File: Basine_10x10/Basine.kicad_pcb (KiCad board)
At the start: 2 copper layers, 100 x 100 mm, 56 parts, among them J1 2060-451/998-404, J10 2060-451/998-404, J11 2060-451/998-404, J12 2060-451/998-404, J13 2060-451/998-404, J14 2060-451/998-404, J15 2060-451/998-404, J16 2060-451/998-404, J17 2060-451/998-404, J18 2060-451/998-404, J2 2060-451/998-404, J3 2060-451/998-404, J4 2060-451/998-404, J5 2060-451/998-404, J6 2060-451/998-404, J7 2060-451/998-404, J8 2060-451/998-404, J9 2060-451/998-404

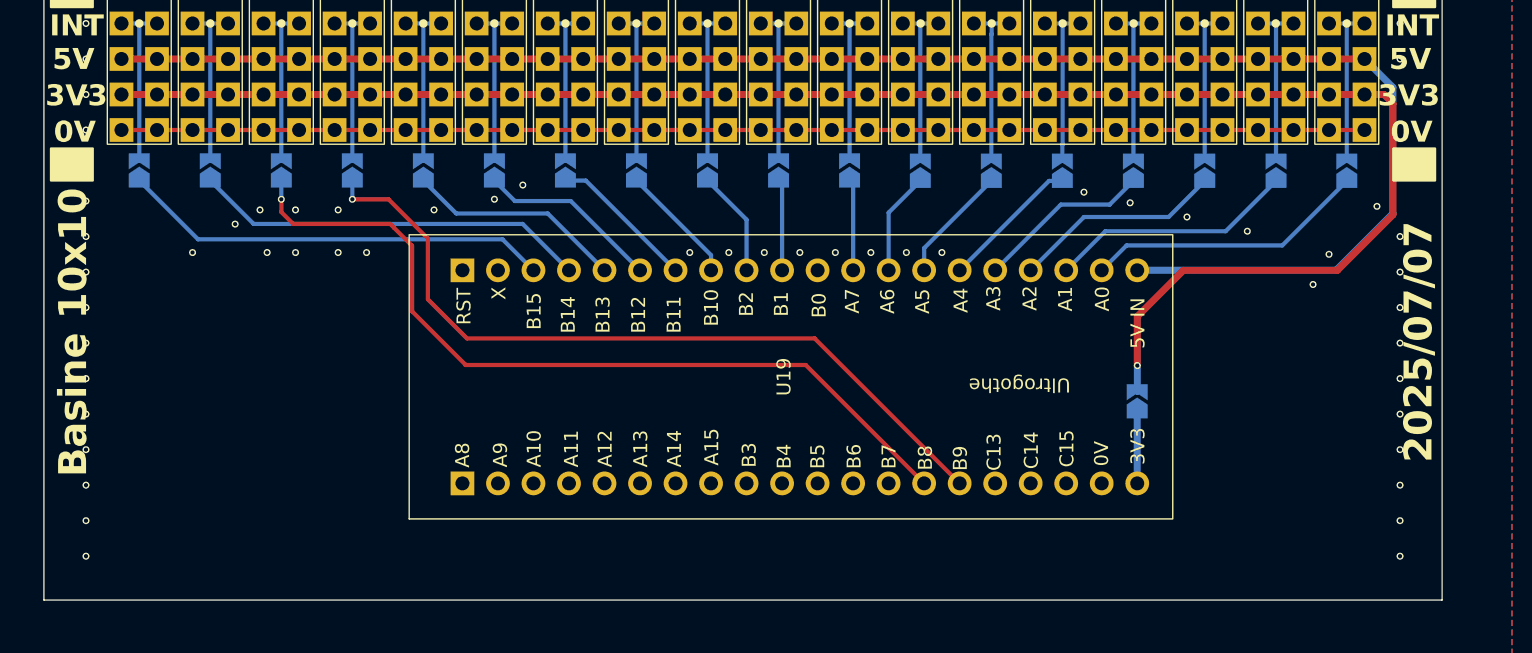
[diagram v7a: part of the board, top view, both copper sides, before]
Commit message: Basine_10x10 : recentrage ultro et ajout zone proto
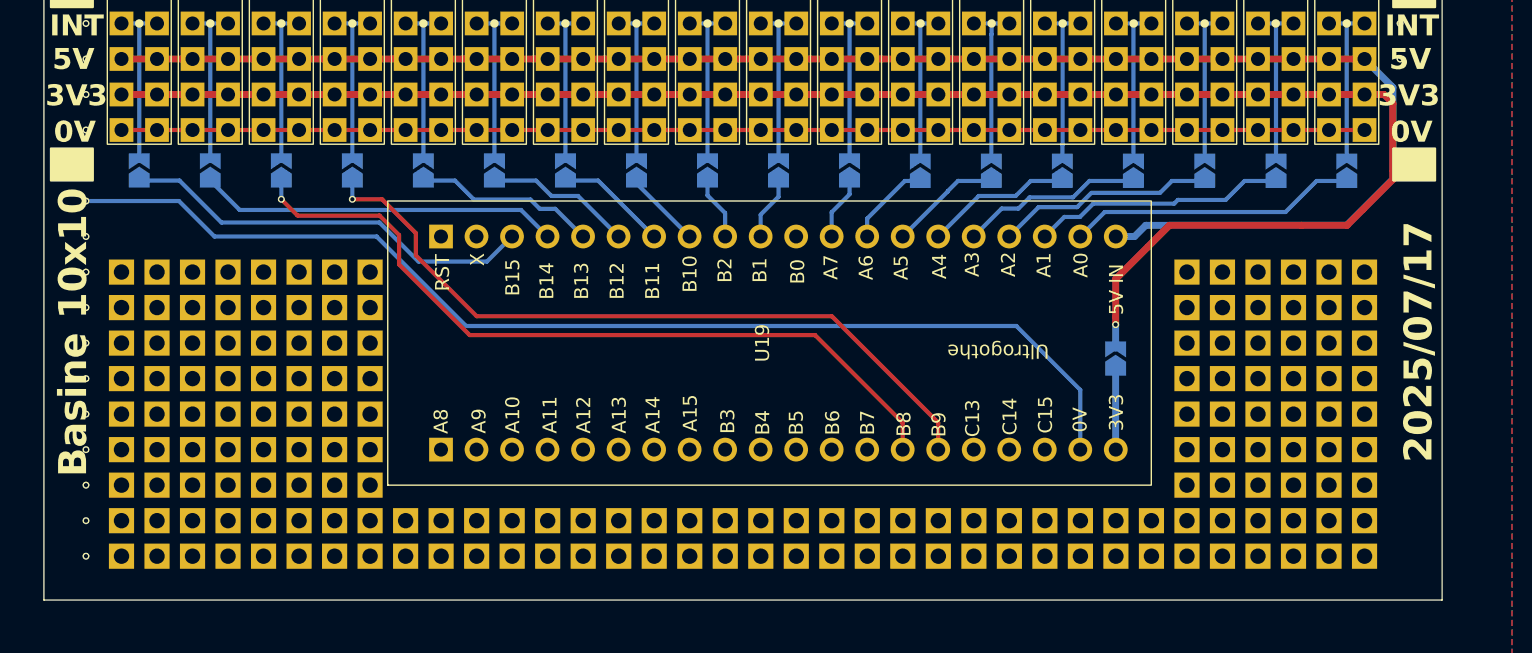
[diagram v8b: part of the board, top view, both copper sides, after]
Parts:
- added J100: Pastille, Chimere_comps:Pastille_carree, F.Cu at (146.2, 194.3)
- added J101: Pastille, Chimere_comps:Pastille_carree, F.Cu at (148.7, 194.3)
- added J102: Pastille, Chimere_comps:Pastille_carree, F.Cu at (151.3, 194.3)
- added J103: Pastille, Chimere_comps:Pastille_carree, F.Cu at (153.8, 194.3)
- added J104: Pastille, Chimere_comps:Pastille_carree, F.Cu at (156.3, 194.3)
- added J105: Pastille, Chimere_comps:Pastille_carree, F.Cu at (158.9, 194.3)
- added J106: Pastille, Chimere_comps:Pastille_carree, F.Cu at (161.4, 194.3)
- added J107: Pastille, Chimere_comps:Pastille_carree, F.Cu at (164.0, 194.3)
- added J108: Pastille, Chimere_comps:Pastille_carree, F.Cu at (166.5, 194.3)
- added J109: Pastille, Chimere_comps:Pastille_carree, F.Cu at (169.1, 194.3)
- added J110: Pastille, Chimere_comps:Pastille_carree, F.Cu at (171.6, 194.3)
- added J111: Pastille, Chimere_comps:Pastille_carree, F.Cu at (174.1, 194.3)
- added J112: Pastille, Chimere_comps:Pastille_carree, F.Cu at (176.7, 194.3)
- added J113: Pastille, Chimere_comps:Pastille_carree, F.Cu at (179.2, 194.3)
- added J114: Pastille, Chimere_comps:Pastille_carree, F.Cu at (125.9, 196.9)
- added J115: Pastille, Chimere_comps:Pastille_carree, F.Cu at (128.4, 196.9)
- added J116: Pastille, Chimere_comps:Pastille_carree, F.Cu at (130.9, 196.9)
- added J117: Pastille, Chimere_comps:Pastille_carree, F.Cu at (133.5, 196.9)
- added J118: Pastille, Chimere_comps:Pastille_carree, F.Cu at (136.0, 196.9)
- added J119: Pastille, Chimere_comps:Pastille_carree, F.Cu at (138.6, 196.9)
- added J120: Pastille, Chimere_comps:Pastille_carree, F.Cu at (141.1, 196.9)
- added J121: Pastille, Chimere_comps:Pastille_carree, F.Cu at (143.7, 196.9)
- added J122: Pastille, Chimere_comps:Pastille_carree, F.Cu at (146.2, 196.9)
- added J123: Pastille, Chimere_comps:Pastille_carree, F.Cu at (148.7, 196.9)
- added J124: Pastille, Chimere_comps:Pastille_carree, F.Cu at (151.3, 196.9)
- added J125: Pastille, Chimere_comps:Pastille_carree, F.Cu at (153.8, 196.9)
- added J126: Pastille, Chimere_comps:Pastille_carree, F.Cu at (156.3, 196.9)
- added J127: Pastille, Chimere_comps:Pastille_carree, F.Cu at (158.9, 196.9)
- added J128: Pastille, Chimere_comps:Pastille_carree, F.Cu at (161.4, 196.9)
- added J129: Pastille, Chimere_comps:Pastille_carree, F.Cu at (164.0, 196.9)
- added J130: Pastille, Chimere_comps:Pastille_carree, F.Cu at (166.5, 196.9)
- added J131: Pastille, Chimere_comps:Pastille_carree, F.Cu at (169.1, 196.9)
- added J132: Pastille, Chimere_comps:Pastille_carree, F.Cu at (171.6, 196.9)
- added J133: Pastille, Chimere_comps:Pastille_carree, F.Cu at (174.1, 196.9)
- added J134: Pastille, Chimere_comps:Pastille_carree, F.Cu at (176.7, 196.9)
- added J135: Pastille, Chimere_comps:Pastille_carree, F.Cu at (194.4, 196.9)
- added J136: Pastille, Chimere_comps:Pastille_carree, F.Cu at (181.8, 176.5)
- added J137: Pastille, Chimere_comps:Pastille_carree, F.Cu at (184.3, 176.5)
- added J138: Pastille, Chimere_comps:Pastille_carree, F.Cu at (186.8, 176.5)
- added J139: Pastille, Chimere_comps:Pastille_carree, F.Cu at (189.4, 176.5)
- added J140: Pastille, Chimere_comps:Pastille_carree, F.Cu at (191.9, 176.5)
- added J141: Pastille, Chimere_comps:Pastille_carree, F.Cu at (194.4, 176.5)
- added J142: Pastille, Chimere_comps:Pastille_carree, F.Cu at (181.8, 179.1)
- added J143: Pastille, Chimere_comps:Pastille_carree, F.Cu at (184.3, 179.1)
- added J144: Pastille, Chimere_comps:Pastille_carree, F.Cu at (186.8, 179.1)
- added J145: Pastille, Chimere_comps:Pastille_carree, F.Cu at (189.4, 179.1)
- added J146: Pastille, Chimere_comps:Pastille_carree, F.Cu at (191.9, 179.1)
- added J147: Pastille, Chimere_comps:Pastille_carree, F.Cu at (194.4, 179.1)
- added J148: Pastille, Chimere_comps:Pastille_carree, F.Cu at (181.8, 181.6)
- added J149: Pastille, Chimere_comps:Pastille_carree, F.Cu at (184.3, 181.6)
- added J150: Pastille, Chimere_comps:Pastille_carree, F.Cu at (186.8, 181.6)
- added J151: Pastille, Chimere_comps:Pastille_carree, F.Cu at (189.4, 181.6)
- added J152: Pastille, Chimere_comps:Pastille_carree, F.Cu at (191.9, 181.6)
- added J153: Pastille, Chimere_comps:Pastille_carree, F.Cu at (194.4, 181.6)
- added J154: Pastille, Chimere_comps:Pastille_carree, F.Cu at (181.8, 184.2)
- added J155: Pastille, Chimere_comps:Pastille_carree, F.Cu at (184.3, 184.2)
- added J156: Pastille, Chimere_comps:Pastille_carree, F.Cu at (186.8, 184.2)
- added J157: Pastille, Chimere_comps:Pastille_carree, F.Cu at (189.4, 184.2)
- added J158: Pastille, Chimere_comps:Pastille_carree, F.Cu at (191.9, 184.2)
- added J159: Pastille, Chimere_comps:Pastille_carree, F.Cu at (194.4, 184.2)
- added J160: Pastille, Chimere_comps:Pastille_carree, F.Cu at (181.8, 186.7)
- added J161: Pastille, Chimere_comps:Pastille_carree, F.Cu at (184.3, 186.7)
- added J162: Pastille, Chimere_comps:Pastille_carree, F.Cu at (186.8, 186.7)
- added J163: Pastille, Chimere_comps:Pastille_carree, F.Cu at (189.4, 186.7)
- added J164: Pastille, Chimere_comps:Pastille_carree, F.Cu at (191.9, 186.7)
- added J165: Pastille, Chimere_comps:Pastille_carree, F.Cu at (194.4, 186.7)
- added J166: Pastille, Chimere_comps:Pastille_carree, F.Cu at (181.8, 189.2)
- added J167: Pastille, Chimere_comps:Pastille_carree, F.Cu at (184.3, 189.2)
- added J168: Pastille, Chimere_comps:Pastille_carree, F.Cu at (186.8, 189.2)
- added J169: Pastille, Chimere_comps:Pastille_carree, F.Cu at (189.4, 189.2)
- added J170: Pastille, Chimere_comps:Pastille_carree, F.Cu at (191.9, 189.2)
- added J171: Pastille, Chimere_comps:Pastille_carree, F.Cu at (194.4, 189.2)
- added J172: Pastille, Chimere_comps:Pastille_carree, F.Cu at (181.8, 191.8)
- added J173: Pastille, Chimere_comps:Pastille_carree, F.Cu at (184.3, 191.8)
- added J174: Pastille, Chimere_comps:Pastille_carree, F.Cu at (186.8, 191.8)
- added J175: Pastille, Chimere_comps:Pastille_carree, F.Cu at (189.4, 191.8)
- added J176: Pastille, Chimere_comps:Pastille_carree, F.Cu at (191.9, 191.8)
- added J177: Pastille, Chimere_comps:Pastille_carree, F.Cu at (194.4, 191.8)
- added J178: Pastille, Chimere_comps:Pastille_carree, F.Cu at (181.8, 194.3)
- added J179: Pastille, Chimere_comps:Pastille_carree, F.Cu at (184.3, 194.3)
- added J180: Pastille, Chimere_comps:Pastille_carree, F.Cu at (186.8, 194.3)
- added J181: Pastille, Chimere_comps:Pastille_carree, F.Cu at (189.4, 194.3)
- added J182: Pastille, Chimere_comps:Pastille_carree, F.Cu at (191.9, 194.3)
- added J183: Pastille, Chimere_comps:Pastille_carree, F.Cu at (194.4, 194.3)
- added J184: Pastille, Chimere_comps:Pastille_carree, F.Cu at (181.8, 196.9)
- added J185: Pastille, Chimere_comps:Pastille_carree, F.Cu at (184.3, 196.9)
- added J186: Pastille, Chimere_comps:Pastille_carree, F.Cu at (186.8, 196.9)
- added J187: Pastille, Chimere_comps:Pastille_carree, F.Cu at (189.4, 196.9)
- added J188: Pastille, Chimere_comps:Pastille_carree, F.Cu at (191.9, 196.9)
- added J19: Pastille, Chimere_comps:Pastille_carree, F.Cu at (123.3, 196.9)
- added J20: Pastille, Chimere_comps:Pastille_carree, F.Cu at (105.5, 176.5)
- added J21: Pastille, Chimere_comps:Pastille_carree, F.Cu at (108.1, 176.5)
- added J22: Pastille, Chimere_comps:Pastille_carree, F.Cu at (110.6, 176.5)
- added J23: Pastille, Chimere_comps:Pastille_carree, F.Cu at (113.2, 176.5)
- added J24: Pastille, Chimere_comps:Pastille_carree, F.Cu at (115.7, 176.5)
- added J25: Pastille, Chimere_comps:Pastille_carree, F.Cu at (118.2, 176.5)
- added J26: Pastille, Chimere_comps:Pastille_carree, F.Cu at (120.8, 176.5)
- added J27: Pastille, Chimere_comps:Pastille_carree, F.Cu at (123.3, 176.5)
- added J28: Pastille, Chimere_comps:Pastille_carree, F.Cu at (105.5, 179.1)
- added J29: Pastille, Chimere_comps:Pastille_carree, F.Cu at (108.1, 179.1)
- added J30: Pastille, Chimere_comps:Pastille_carree, F.Cu at (110.6, 179.1)
- added J31: Pastille, Chimere_comps:Pastille_carree, F.Cu at (113.2, 179.1)
- added J32: Pastille, Chimere_comps:Pastille_carree, F.Cu at (115.7, 179.1)
- added J33: Pastille, Chimere_comps:Pastille_carree, F.Cu at (118.2, 179.1)
- added J34: Pastille, Chimere_comps:Pastille_carree, F.Cu at (120.8, 179.1)
- added J35: Pastille, Chimere_comps:Pastille_carree, F.Cu at (123.3, 179.1)
- added J36: Pastille, Chimere_comps:Pastille_carree, F.Cu at (105.5, 181.6)
- added J37: Pastille, Chimere_comps:Pastille_carree, F.Cu at (108.1, 181.6)
- added J38: Pastille, Chimere_comps:Pastille_carree, F.Cu at (110.6, 181.6)
- added J39: Pastille, Chimere_comps:Pastille_carree, F.Cu at (113.2, 181.6)
- added J40: Pastille, Chimere_comps:Pastille_carree, F.Cu at (115.7, 181.6)
- added J41: Pastille, Chimere_comps:Pastille_carree, F.Cu at (118.2, 181.6)
- added J42: Pastille, Chimere_comps:Pastille_carree, F.Cu at (120.8, 181.6)
- added J43: Pastille, Chimere_comps:Pastille_carree, F.Cu at (123.3, 181.6)
- added J44: Pastille, Chimere_comps:Pastille_carree, F.Cu at (105.5, 184.2)
- added J45: Pastille, Chimere_comps:Pastille_carree, F.Cu at (108.1, 184.2)
- added J46: Pastille, Chimere_comps:Pastille_carree, F.Cu at (110.6, 184.2)
- added J47: Pastille, Chimere_comps:Pastille_carree, F.Cu at (113.2, 184.2)
- added J48: Pastille, Chimere_comps:Pastille_carree, F.Cu at (115.7, 184.2)
- added J49: Pastille, Chimere_comps:Pastille_carree, F.Cu at (118.2, 184.2)
- added J50: Pastille, Chimere_comps:Pastille_carree, F.Cu at (120.8, 184.2)
- added J51: Pastille, Chimere_comps:Pastille_carree, F.Cu at (123.3, 184.2)
- added J52: Pastille, Chimere_comps:Pastille_carree, F.Cu at (105.5, 186.7)
- added J53: Pastille, Chimere_comps:Pastille_carree, F.Cu at (108.1, 186.7)
- added J54: Pastille, Chimere_comps:Pastille_carree, F.Cu at (110.6, 186.7)
- added J55: Pastille, Chimere_comps:Pastille_carree, F.Cu at (113.2, 186.7)
- added J56: Pastille, Chimere_comps:Pastille_carree, F.Cu at (115.7, 186.7)
- added J57: Pastille, Chimere_comps:Pastille_carree, F.Cu at (118.2, 186.7)
- added J58: Pastille, Chimere_comps:Pastille_carree, F.Cu at (120.8, 186.7)
- added J59: Pastille, Chimere_comps:Pastille_carree, F.Cu at (123.3, 186.7)
- added J60: Pastille, Chimere_comps:Pastille_carree, F.Cu at (105.5, 189.2)
- added J61: Pastille, Chimere_comps:Pastille_carree, F.Cu at (108.1, 189.2)
- added J62: Pastille, Chimere_comps:Pastille_carree, F.Cu at (110.6, 189.2)
- added J63: Pastille, Chimere_comps:Pastille_carree, F.Cu at (113.2, 189.2)
- added J64: Pastille, Chimere_comps:Pastille_carree, F.Cu at (115.7, 189.2)
- added J65: Pastille, Chimere_comps:Pastille_carree, F.Cu at (118.2, 189.2)
- added J66: Pastille, Chimere_comps:Pastille_carree, F.Cu at (120.8, 189.2)
- added J67: Pastille, Chimere_comps:Pastille_carree, F.Cu at (123.3, 189.2)
- added J68: Pastille, Chimere_comps:Pastille_carree, F.Cu at (105.5, 191.8)
- added J69: Pastille, Chimere_comps:Pastille_carree, F.Cu at (108.1, 191.8)
- added J70: Pastille, Chimere_comps:Pastille_carree, F.Cu at (110.6, 191.8)
- added J71: Pastille, Chimere_comps:Pastille_carree, F.Cu at (113.2, 191.8)
- added J72: Pastille, Chimere_comps:Pastille_carree, F.Cu at (115.7, 191.8)
- added J73: Pastille, Chimere_comps:Pastille_carree, F.Cu at (118.2, 191.8)
- added J74: Pastille, Chimere_comps:Pastille_carree, F.Cu at (120.8, 191.8)
- added J75: Pastille, Chimere_comps:Pastille_carree, F.Cu at (123.3, 191.8)
- added J76: Pastille, Chimere_comps:Pastille_carree, F.Cu at (105.5, 194.3)
- added J77: Pastille, Chimere_comps:Pastille_carree, F.Cu at (108.1, 194.3)
- added J78: Pastille, Chimere_comps:Pastille_carree, F.Cu at (110.6, 194.3)
- added J79: Pastille, Chimere_comps:Pastille_carree, F.Cu at (113.2, 194.3)
- added J80: Pastille, Chimere_comps:Pastille_carree, F.Cu at (115.7, 194.3)
- added J81: Pastille, Chimere_comps:Pastille_carree, F.Cu at (118.2, 194.3)
- added J82: Pastille, Chimere_comps:Pastille_carree, F.Cu at (120.8, 194.3)
- added J83: Pastille, Chimere_comps:Pastille_carree, F.Cu at (123.3, 194.3)
- added J84: Pastille, Chimere_comps:Pastille_carree, F.Cu at (105.5, 196.9)
- added J85: Pastille, Chimere_comps:Pastille_carree, F.Cu at (108.1, 196.9)
- added J86: Pastille, Chimere_comps:Pastille_carree, F.Cu at (110.6, 196.9)
- added J87: Pastille, Chimere_comps:Pastille_carree, F.Cu at (113.2, 196.9)
- added J88: Pastille, Chimere_comps:Pastille_carree, F.Cu at (115.7, 196.9)
- added J89: Pastille, Chimere_comps:Pastille_carree, F.Cu at (118.2, 196.9)
- added J90: Pastille, Chimere_comps:Pastille_carree, F.Cu at (120.8, 196.9)
- added J91: Pastille, Chimere_comps:Pastille_carree, F.Cu at (179.2, 196.9)
- added J92: Pastille, Chimere_comps:Pastille_carree, F.Cu at (125.9, 194.3)
- added J93: Pastille, Chimere_comps:Pastille_carree, F.Cu at (128.4, 194.3)
- added J94: Pastille, Chimere_comps:Pastille_carree, F.Cu at (130.9, 194.3)
- added J95: Pastille, Chimere_comps:Pastille_carree, F.Cu at (133.5, 194.3)
- added J96: Pastille, Chimere_comps:Pastille_carree, F.Cu at (136.0, 194.3)
- added J97: Pastille, Chimere_comps:Pastille_carree, F.Cu at (138.6, 194.3)
- added J98: Pastille, Chimere_comps:Pastille_carree, F.Cu at (141.1, 194.3)
- added J99: Pastille, Chimere_comps:Pastille_carree, F.Cu at (143.7, 194.3)
- moved JP19 3.43 mm to (176.7, 182.7)
- moved U19 2.86 mm to (151.9, 181.6)
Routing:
- net 0V: track 197.9 -> 278.9 mm, vias 99 -> 62
- net CAN_RX: track 59.0 -> 55.5 mm
- net B10: track 8.63 -> 5.57 mm
- net B2: track 7.57 -> 4.52 mm
- net CAN_TX: track 55.7 -> 52.7 mm
- net B11: track 10.5 -> 8.00 mm
- net B12: track 13.1 -> 10.5 mm
- net B14: track 28.3 -> 25.8 mm
- net B13: track 15.6 -> 13.1 mm
- net A7: track 6.52 -> 4.89 mm
- net B1: track 6.52 -> 4.89 mm
- net 3V3: track 125.8 -> 124.4 mm
- net A6: track 7.33 -> 6.20 mm
- net B15: track 30.9 -> 29.8 mm
- net 5V: track 120.8 -> 119.9 mm
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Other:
- board text added: "2025/07/17"
- board text removed: "2025/07/07"
